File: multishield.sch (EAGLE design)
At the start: 1 part, among them J1 ARDUINO_R3_SHIELD

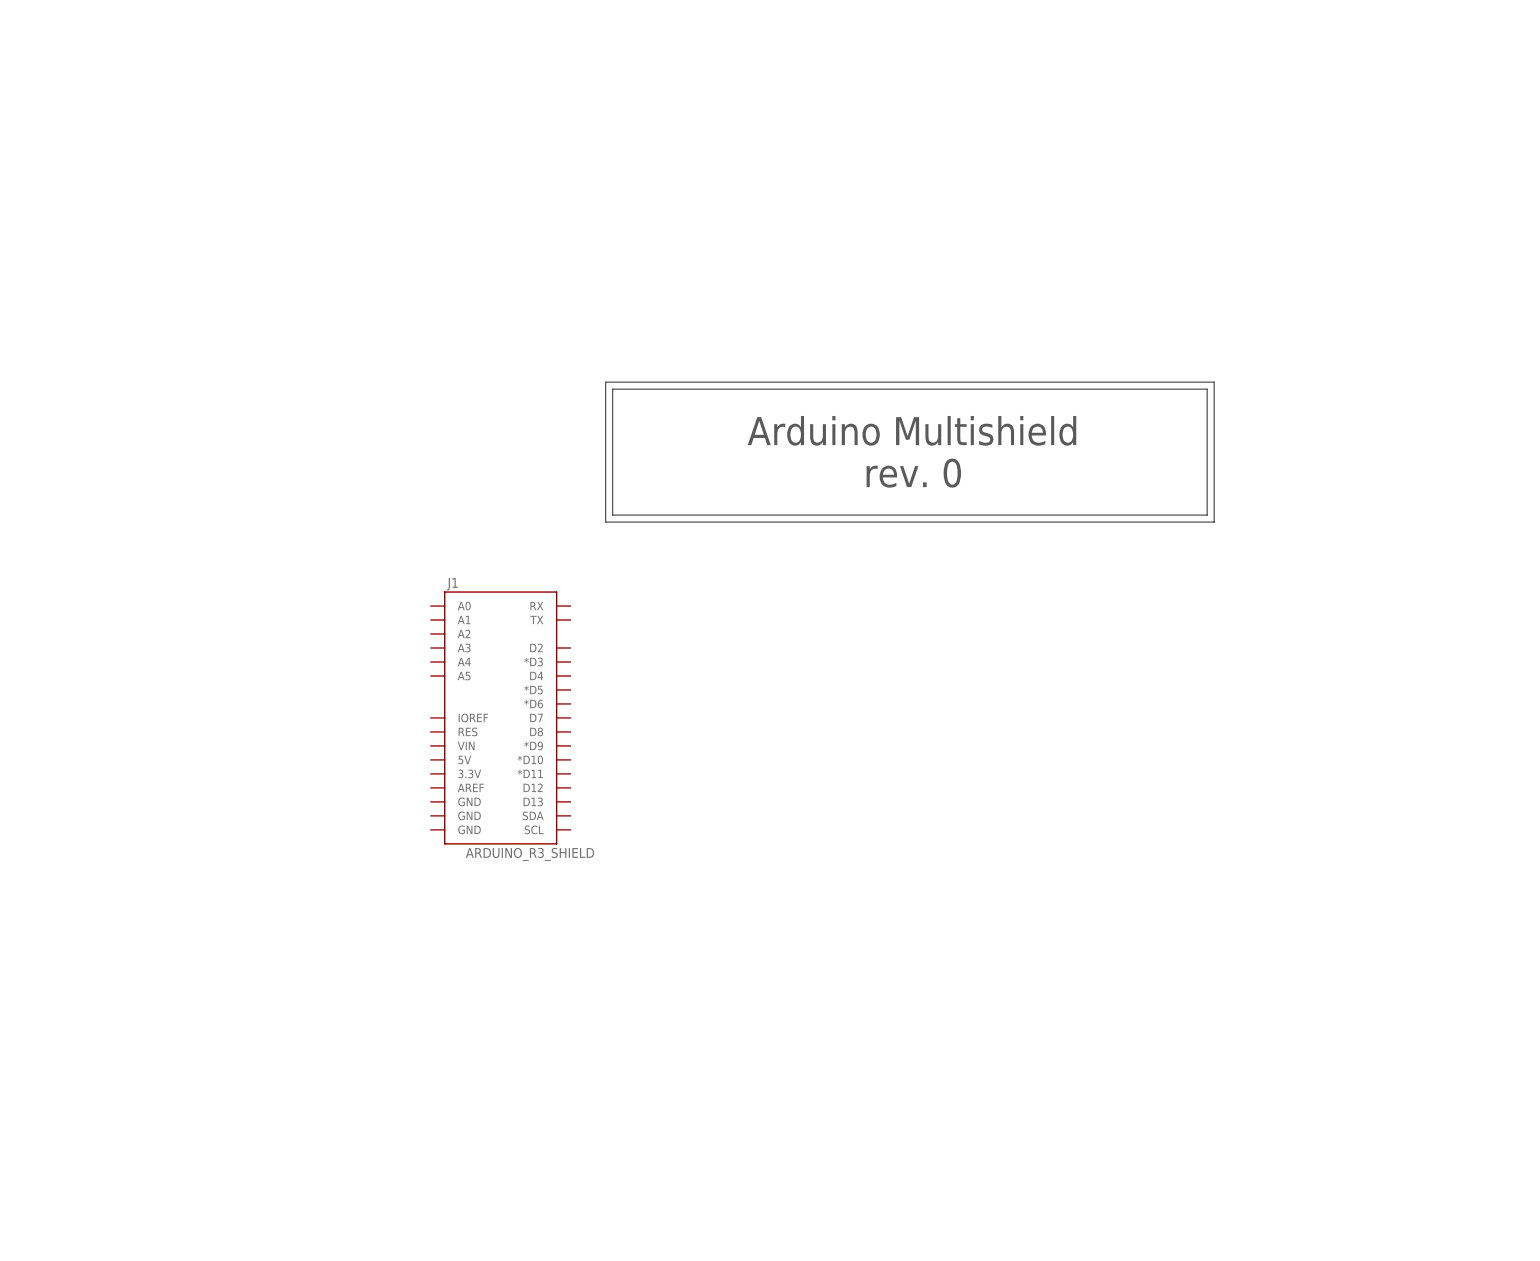
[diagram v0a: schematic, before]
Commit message: adding shield with breakouts
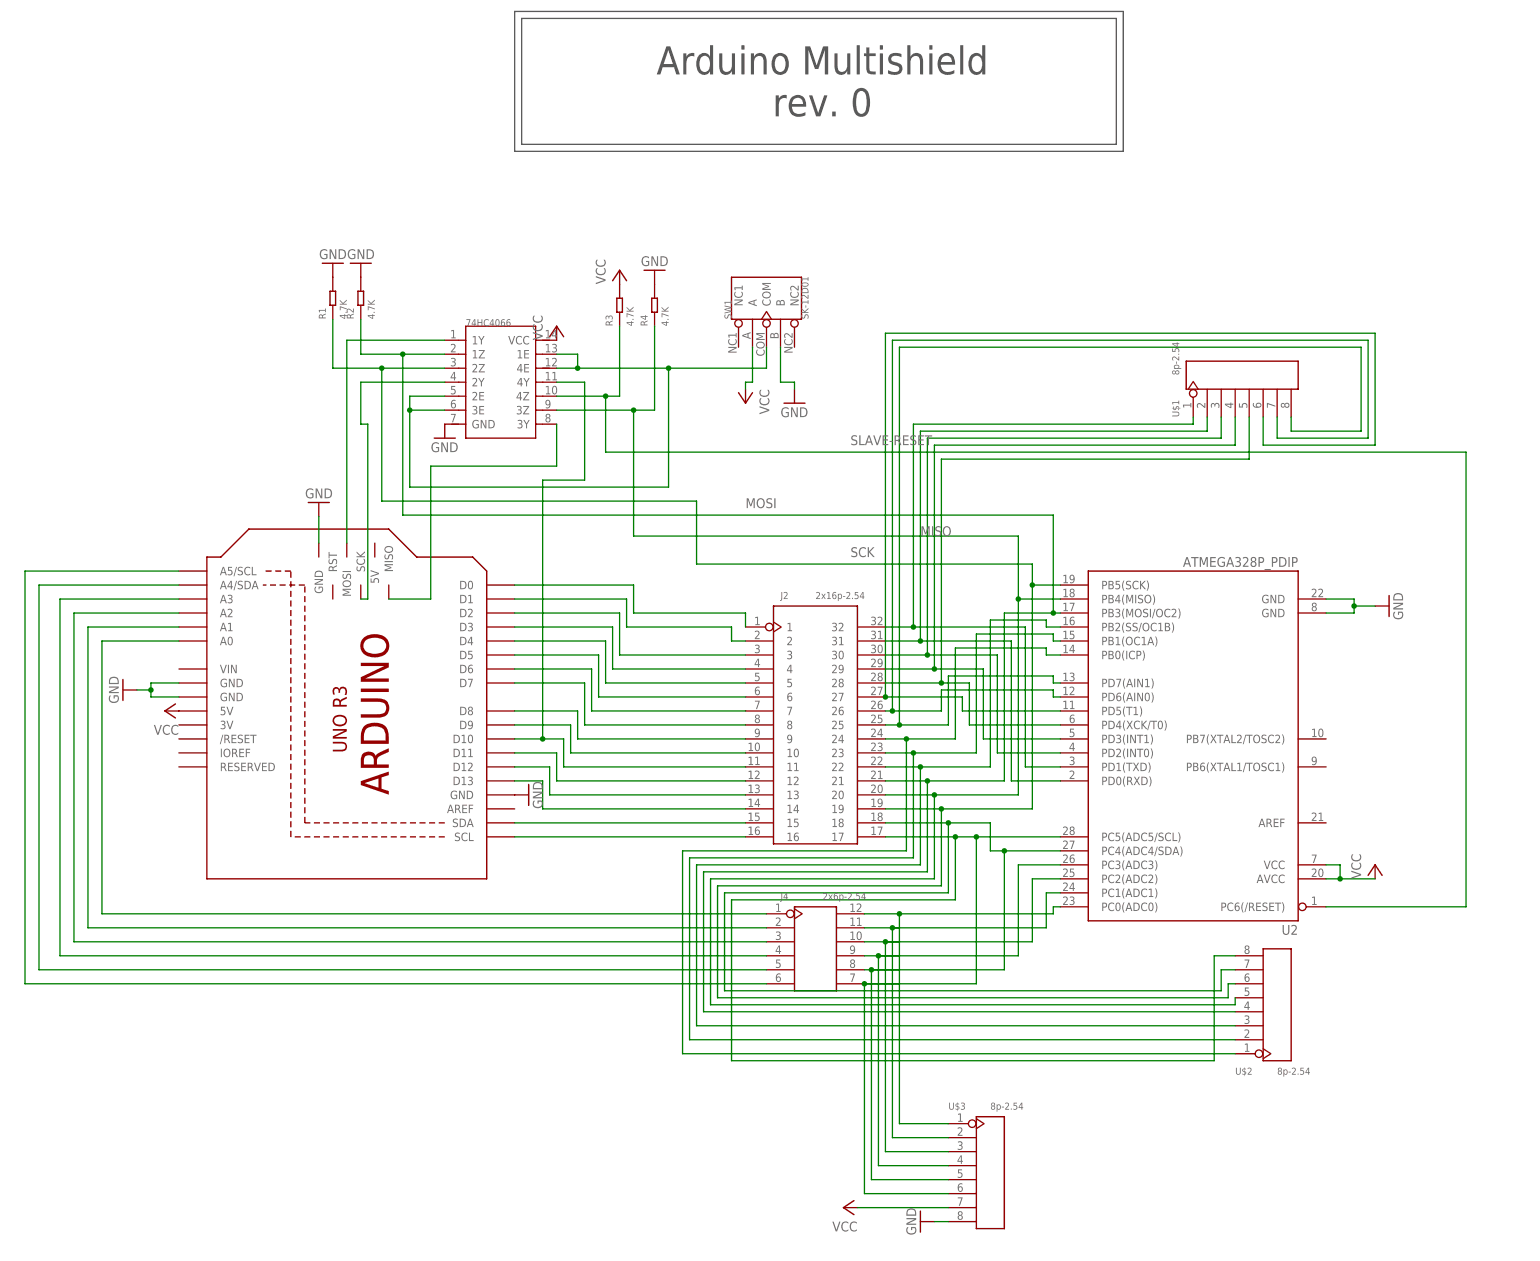
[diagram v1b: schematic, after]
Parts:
- removed J1: ARDUINO_R3_SHIELD, SparkFun-Boards:ARDUINO_R3_SHIELD
- added J2: 2x16p-2.54, Seeed-OPL-Connector:DIP-BLACK-MALE-HEADER-VERT(2X16P-2.54)
- added J4: 2x6p-2.54, Seeed-OPL-Connector:DIP-BLACK-MALE-HEADER(2X6P-2.54)
- added M1: ARDUINO_R3_ICSP, adafruit:ARDUINO_R3_ICSP
- added R1, R2, R3, R4: 4.7K, Seeed-OPL-Resistor:DIP-RES-4.7K-5%-1/4W(PR-D2.3XL6.5MM)
- added SW1: SK-12D01, Seeed-OPL-Button:DIP-TOGGLE-SWITCH-ON-ON(3+2P-8.8X4.6MM)
- added U$1, U$2, U$3: 8p-2.54, Seeed-OPL-Connector:DIP-BLACK-MALE-HEADER-VERT(8P-2.54)
- added U1: AD595AQ-DIP14, Seeed-OPL-ic:74HC4066(DIP14)
- added U2: ATMEGA328P_PDIP, SparkFun-DigitalIC:ATMEGA328P_PDIP
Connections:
- new net GND: M1.GND, M1.GND@1, M1.GND@2, M1.GND@3, R1.2, R2.2, R4.2, SW1.B, U$3.8, U1.GND, U2.GND@1, U2.GND@2
- new net MISO: J2.20, R4.1, U$2.5, U1.3Z, U2.PB4(MISO)
- new net MOSI: J2.21, R2.1, U$2.4, U1.1Z, U2.PB3(MOSI/OC2)
- new net N$11: J2.3, M1.D2
- new net N$12: J2.4, M1.D3
- new net N$13: J2.5, M1.D4
- new net N$14: J2.6, M1.D5
- new net N$15: J2.7, M1.D6
- new net N$16: J2.8, M1.D7
- new net N$17: J2.9, M1.D8
- new net N$18: J2.10, M1.D9
- new net N$19: J2.11, M1.D10, U1.4Y
- new net N$2: J2.1, M1.D0
- new net N$20: J2.12, M1.D11
- new net N$21: J2.13, M1.D12
- new net N$22: J2.14, M1.D13
- new net N$23: J2.15, M1.SDA
- new net N$24: J2.16, M1.SCL
- new net N$25: J2.32, U$1.1, U2.PD1(TXD)
- new net N$26: J2.31, U$1.2, U2.PD0(RXD)
- new net N$27: J2.30, U$1.3, U2.PD2(INT0)
- new net N$28: J2.29, U$1.4, U2.PD3(INT1)
- new net N$29: J2.28, U$1.5, U2.PD4(XCK/T0)
- new net N$30: J2.27, U$1.6, U2.PD5(T1)
- new net N$31: J4.1, M1.A0
- new net N$32: J2.25, U$1.8, U2.PD7(AIN1)
- new net N$33: J2.24, U$2.1, U2.PB0(ICP)
- new net N$34: J2.23, U$2.2, U2.PB1(OC1A)
- new net N$35: J2.22, U$2.3, U2.PB2(SS/OC1B)
- new net N$39: M1.MOSI, U1.1Y
- new net N$40: M1.SCK, U1.2Y
- new net N$41: J2.26, U$1.7, U2.PD6(AIN0)
- new net N$42: J4.2, M1.A1
- new net N$43: J4.3, M1.A2
- new net N$44: J4.4, M1.A3
- new net N$45: J4.12, U$3.1, U2.PC0(ADC0)
- new net N$46: J4.11, U$3.2, U2.PC1(ADC1)
- new net N$47: J4.10, U$3.3, U2.PC2(ADC2)
- new net N$48: J4.9, U$3.4, U2.PC3(ADC3)
- new net N$49: J2.18, J4.8, U$2.7, U$3.5, U2.PC4(ADC4/SDA)
- new net N$50: J2.17, J4.7, U$2.8, U$3.6, U2.PC5(ADC5/SCL)
- new net N$51: J4.5, M1.A4/SDA
- new net N$52: J4.6, M1.A5/SCL
- new net N$53: M1.MISO, U1.3Y
- new net N$56: SW1.COM, U1.1E, U1.2E, U1.3E, U1.4E
- new net N$9: J2.2, M1.D1
- new net SCK: J2.19, R1.1, U$2.6, U1.2Z, U2.PB5(SCK)
- new net SLAVE-RESET: R3.1, U1.4Z, U2.PC6(/RESET)
- new net VCC: M1.5V, R3.2, SW1.A, U$3.7, U1.VCC, U2.AVCC, U2.VCC
